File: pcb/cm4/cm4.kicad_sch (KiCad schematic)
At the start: 2 parts, among them J101 Conn_01x05, J102 Conn_01x07

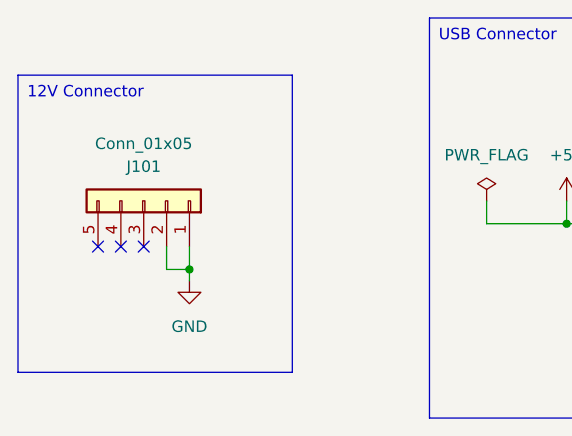
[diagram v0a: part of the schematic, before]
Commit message: fix power pin issue
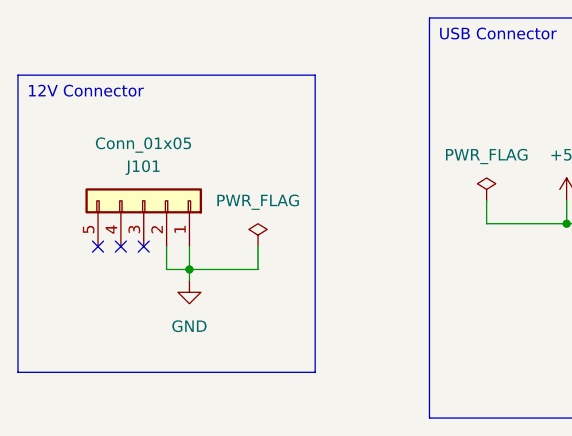
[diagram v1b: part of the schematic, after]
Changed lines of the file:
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@@
+	(wire
+		(pts
+			(xy 85.09 91.44) (xy 92.71 91.44)
+		)
+		(stroke
+			(width 0)
+			(type default)
+		)
+	)
 	(wire
 		(pts
@@
 	(wire
 		(pts
+			(xy 92.71 88.9) (xy 92.71 91.44)
+		)
+		(stroke
+			(width 0)
+			(type default)
+		)
+	)
+	(wire
+		(pts
 			(xy 85.09 91.44) (xy 85.09 92.71)
 		)
@@
 		(exclude_from_sim no)
 		(at 66.04 69.85 0)
-		(size 30.48 33.02)
+		(size 33.02 33.02)
 		(stroke
 			(width 0)
@@
 					(unit 1)
 				)
+			)
+		)
+	)
+	(symbol
+		(lib_id "power:PWR_FLAG")
+		(at 92.71 88.9 0)
+		(unit 1)
+		(exclude_from_sim no)
+		(in_bom yes)
+		(on_board yes)
+		(dnp no)
+		(fields_autoplaced yes)
+		(property "Reference" "#FLG0102"
+			(at 92.71 86.995 0)
+			(effects
+				(font
+					(size 1.27 1.27)
+				)
+				(hide yes)
+			)
+		)
+		(property "Value" "PWR_FLAG"
+			(at 92.71 83.82 0)
+			(effects
+				(font
+					(size 1.27 1.27)
+				)
+			)
+		)
+		(property "Footprint" ""
+			(at 92.71 88.9 0)
+			(effects
+				(font
+					(size 1.27 1.27)
+				)
+				(hide yes)
+			)
+		)
+		(property "Datasheet" "~"
+			(at 92.71 88.9 0)
+			(effects
+				(font
+					(size 1.27 1.27)
+				)
+				(hide yes)
+			)
+		)
+		(property "Description" "Special symbol for telling ERC where power comes from"
+			(at 92.71 88.9 0)
+			(effects
+				(font
+					(size 1.27 1.27)
+				)
+				(hide yes)
+			)
+		)
+		(pin "1"
+		)
+		(instances
+			(project "cm4"
+				(path "/5d20b266-567e-45c6-9e3e-145c2aea1daa"
+					(reference "#FLG0102")
+					(unit 1)
+				)

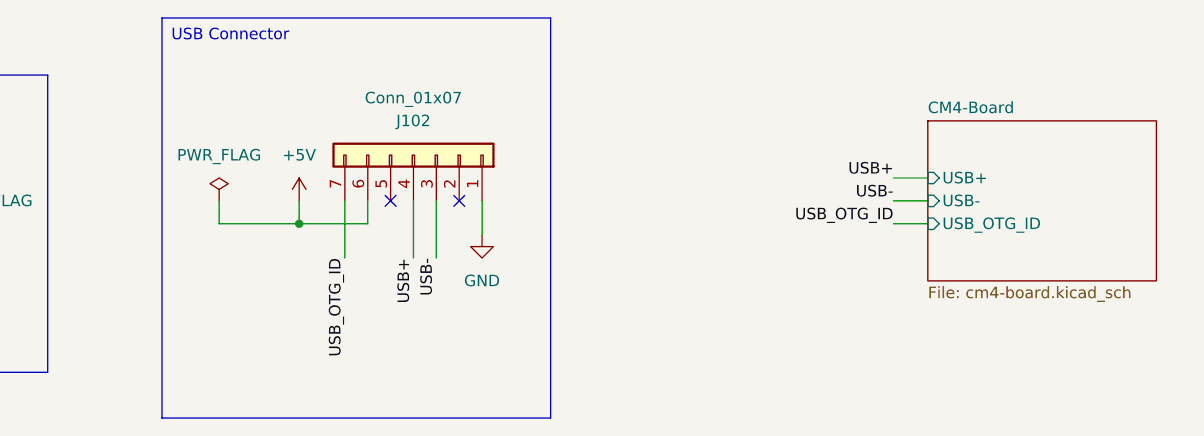
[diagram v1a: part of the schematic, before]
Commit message: update connectors
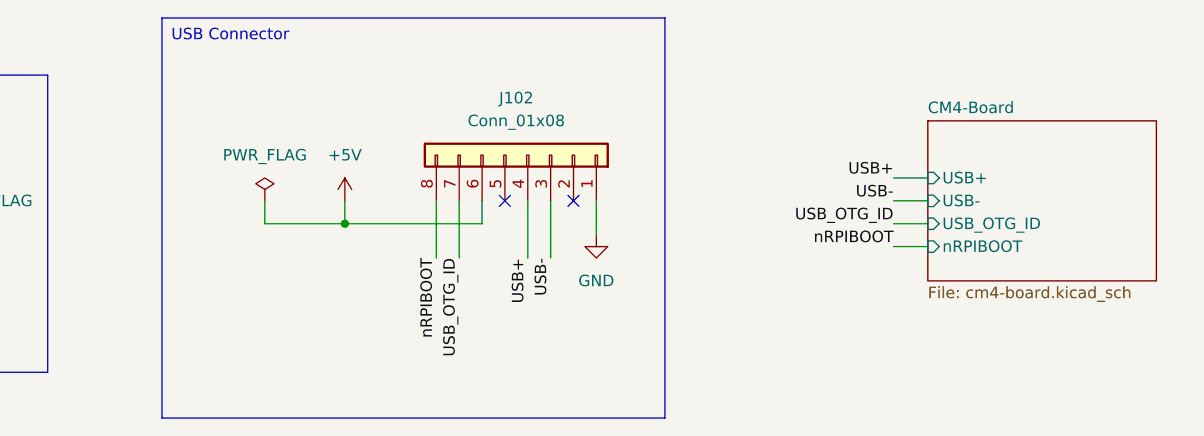
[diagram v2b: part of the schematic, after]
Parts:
- removed J102: Conn_01x07, symbol Connector_Generic:Conn_01x07
- added J102: Conn_01x08, symbol Connector_Generic:Conn_01x08
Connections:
- net +5V: now also J102.6 (Pin_6)
- net GND: now also J102.1 (Pin_1)
- net USB+: now also J102.4 (Pin_4)
- net USB-: now also J102.3 (Pin_3)
- net USB_OTG_ID: now also J102.7 (Pin_7)
- new net nRPIBOOT: J102.8 (Pin_8)
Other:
- sheet CM4-Board ports: added nRPIBOOT; removed none
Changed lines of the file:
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@@
 	)
 	(junction
-		(at 127 86.36)
+		(at 132.08 86.36)
 		(diameter 0)
 		(color 0 0 0 0)
@@
 	)
 	(no_connect
-		(at 137.16 83.82)
+		(at 149.86 83.82)
 	)
 	(no_connect
-		(at 144.78 83.82)
+		(at 157.48 83.82)
 	)
 	(no_connect
@@
 	(wire
 		(pts
-			(xy 139.7 90.17) (xy 139.7 83.82)
-		)
-		(stroke
-			(width 0)
-			(type default)
-		)
-	)
-	(wire
-		(pts
-			(xy 118.11 83.82) (xy 118.11 86.36)
-		)
-		(stroke
-			(width 0)
-			(type default)
-		)
-	)
-	(wire
-		(pts
-			(xy 127 83.82) (xy 127 86.36)
-		)
-		(stroke
-			(width 0)
-			(type default)
-		)
-	)
-	(wire
-		(pts
-			(xy 147.32 83.82) (xy 147.32 87.63)
+			(xy 152.4 90.17) (xy 152.4 83.82)
+		)
+		(stroke
+			(width 0)
+			(type default)
+		)
+	)
+	(wire
+		(pts
+			(xy 123.19 83.82) (xy 123.19 86.36)
+		)
+		(stroke
+			(width 0)
+			(type default)
+		)
+	)
+	(wire
+		(pts
+			(xy 132.08 83.82) (xy 132.08 86.36)
+		)
+		(stroke
+			(width 0)
+			(type default)
+		)
+	)
+	(wire
+		(pts
+			(xy 193.04 88.9) (xy 196.85 88.9)
+		)
+		(stroke
+			(width 0)
+			(type default)
+		)
+	)
+	(wire
+		(pts
+			(xy 160.02 83.82) (xy 160.02 87.63)
+		)
+		(stroke
+			(width 0)
+			(type default)
+		)
+	)
+	(wire
+		(pts
+			(xy 142.24 83.82) (xy 142.24 90.17)
 		)
 		(stroke
@@
 	(wire
 		(pts
-			(xy 134.62 83.82) (xy 134.62 86.36)
-		)
-		(stroke
-			(width 0)
-			(type default)
-		)
-	)
-	(wire
-		(pts
-			(xy 118.11 86.36) (xy 127 86.36)
-		)
-		(stroke
-			(width 0)
-			(type default)
-		)
-	)
-	(wire
-		(pts
-			(xy 142.24 90.17) (xy 142.24 83.82)
+			(xy 147.32 83.82) (xy 147.32 86.36)
+		)
+		(stroke
+			(width 0)
+			(type default)
+		)
+	)
+	(wire
+		(pts
+			(xy 123.19 86.36) (xy 132.08 86.36)
+		)
+		(stroke
+			(width 0)
+			(type default)
+		)
+	)
+	(wire
+		(pts
+			(xy 154.94 90.17) (xy 154.94 83.82)
 		)
 		(stroke
@@
 	(wire
 		(pts
-			(xy 134.62 86.36) (xy 127 86.36)
+			(xy 147.32 86.36) (xy 132.08 86.36)
 		)
 		(stroke
@@
 	(wire
 		(pts
-			(xy 132.08 83.82) (xy 132.08 90.17)
+			(xy 144.78 83.82) (xy 144.78 90.17)
 		)
 		(stroke
@@
 		(exclude_from_sim no)
 		(at 111.76 63.5 0)
-		(size 43.18 44.45)
+		(size 55.88 44.45)
 		(stroke
 			(width 0)
@@
 	)
 	(label "USB_OTG_ID"
-		(at 132.08 90.17 270)
+		(at 144.78 90.17 270)
 		(fields_autoplaced yes)
 		(effects
@@
 	)
 	(label "USB+"
-		(at 139.7 90.17 270)
+		(at 152.4 90.17 270)
 		(fields_autoplaced yes)
 		(effects
@@
 		)
 	)
+	(label "nRPIBOOT"
+		(at 193.04 88.9 180)
+		(fields_autoplaced yes)
+		(effects
+			(font
+				(size 1.27 1.27)
+			)
+			(justify right bottom)
+		)
+	)
+	(label "nRPIBOOT"
+		(at 142.24 90.17 270)
+		(fields_autoplaced yes)
+		(effects
+			(font
+				(size 1.27 1.27)
+			)
+			(justify right bottom)
+		)
+	)
 	(label "USB-"
-		(at 142.24 90.17 270)
+		(at 154.94 90.17 270)
 		(fields_autoplaced yes)
 		(effects
@@
 	(symbol
 		(lib_id "power:GND")
-		(at 147.32 87.63 0)
+		(at 160.02 87.63 0)
 		(unit 1)
 		(exclude_from_sim no)
@@
 		(fields_autoplaced yes)
 		(property "Reference" "#PWR0103"
-			(at 147.32 93.98 0)
+			(at 160.02 93.98 0)
 			(effects
 				(font
@@
 		)
 		(property "Value" "GND"
-			(at 147.32 92.71 0)
+			(at 160.02 92.71 0)
 			(effects
 				(font
@@
 		)
 		(property "Footprint" ""
-			(at 147.32 87.63 0)
+			(at 160.02 87.63 0)
 			(effects
 				(font
@@
 		)
 		(property "Datasheet" ""
-			(at 147.32 87.63 0)
+			(at 160.02 87.63 0)
 			(effects
 				(font
@@
 		)
 		(property "Description" "Power symbol creates a global label with name \"GND\" , ground"
-			(at 147.32 87.63 0)
+			(at 160.02 87.63 0)
 			(effects
 				(font
@@
 	)
 	(symbol
-		(lib_id "Connector_Generic:Conn_01x07")
-		(at 139.7 78.74 270)
+		(lib_id "Connector_Generic:Conn_01x08")
+		(at 152.4 78.74 270)
 		(mirror x)
 		(unit 1)
@@
 		(dnp no)
 		(property "Reference" "J102"
-			(at 139.7 74.93 90)
-			(effects
-				(font
-					(size 1.27 1.27)
-				)
-			)
-		)
-		(property "Value" "Conn_01x07"
-			(at 139.7 72.39 90)
+			(at 151.13 72.39 90)
+			(effects
+				(font
+					(size 1.27 1.27)
+				)
+			)
+		)
+		(property "Value" "Conn_01x08"
+			(at 151.13 74.93 90)
 			(effects
 				(font
@@
 		)
 		(property "Footprint" ""
-			(at 139.7 78.74 0)
+			(at 152.4 78.74 0)
 			(effects
 				(font
@@
 		)
 		(property "Datasheet" "~"
-			(at 139.7 78.74 0)
-			(effects
-				(font
-					(size 1.27 1.27)
-				)
-				(hide yes)
-			)
-		)
-		(property "Description" "Generic connector, single row, 01x07, script generated (kicad-library-utils/schlib/autogen/connector/)"
-			(at 139.7 78.74 0)
-			(effects
-				(font
-					(size 1.27 1.27)
-				)
-				(hide yes)
-			)
+			(at 152.4 78.74 0)
+			(effects
+				(font
+					(size 1.27 1.27)
+				)
+				(hide yes)
+			)
+		)
+		(property "Description" "Generic connector, single row, 01x08, script generated (kicad-library-utils/schlib/autogen/connector/)"
+			(at 152.4 78.74 0)
+			(effects
+				(font
+					(size 1.27 1.27)
+				)
+				(hide yes)
+			)
+		)
+		(pin "2"
 		)
 		(pin "3"
 		)
+		(pin "7"
+		)
+		(pin "6"
+		)
+		(pin "4"
+		)
+		(pin "1"
+		)
+		(pin "8"
+		)
 		(pin "5"
-		)
-		(pin "2"
-		)
-		(pin "4"
-		)
-		(pin "1"
-		)
-		(pin "6"
-		)
-		(pin "7"
 		)
 		(instances
@@
 	(symbol
 		(lib_id "power:+5V")
-		(at 127 83.82 0)
+		(at 132.08 83.82 0)
 		(unit 1)
 		(exclude_from_sim no)
@@
 		(fields_autoplaced yes)
 		(property "Reference" "#PWR0102"
-			(at 127 87.63 0)
+			(at 132.08 87.63 0)
 			(effects
 				(font
@@
 		)
 		(property "Value" "+5V"
-			(at 127 78.74 0)
+			(at 132.08 78.74 0)
 			(effects
 				(font
@@
 		)
 		(property "Footprint" ""
-			(at 127 83.82 0)
+			(at 132.08 83.82 0)
 			(effects
 				(font
@@
 		)
 		(property "Datasheet" ""
-			(at 127 83.82 0)
+			(at 132.08 83.82 0)
 			(effects
 				(font
@@
 		)
 		(property "Description" "Power symbol creates a global label with name \"+5V\""
-			(at 127 83.82 0)
+			(at 132.08 83.82 0)
 			(effects
 				(font
@@
 	(symbol
 		(lib_id "power:PWR_FLAG")
-		(at 118.11 83.82 0)
+		(at 123.19 83.82 0)
 		(unit 1)
 		(exclude_from_sim no)
@@
 		(fields_autoplaced yes)
 		(property "Reference" "#FLG0101"
-			(at 118.11 81.915 0)
+			(at 123.19 81.915 0)
 			(effects
 				(font
@@
 		)
 		(property "Value" "PWR_FLAG"
-			(at 118.11 78.74 0)
+			(at 123.19 78.74 0)
 			(effects
 				(font
@@
 		)
 		(property "Footprint" ""
-			(at 118.11 83.82 0)
+			(at 123.19 83.82 0)
 			(effects
 				(font
@@
 		)
 		(property "Datasheet" "~"
-			(at 118.11 83.82 0)
+			(at 123.19 83.82 0)
 			(effects
 				(font
@@
 		)
 		(property "Description" "Special symbol for telling ERC where power comes from"
-			(at 118.11 83.82 0)
+			(at 123.19 83.82 0)
 			(effects
 				(font
@@
 			(effects
 				(font
+					(size 1.27 1.27)
+				)
+				(justify left)
+			)
+		)
+		(pin "nRPIBOOT" input
+			(at 196.85 88.9 180)
+			(effects
+				(font

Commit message: update cm4
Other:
- added sheet Ethernet (ethernet.kicad_sch)
- added sheet MicroSD (micro_sd.kicad_sch)
- sheet CM4-Board ports: added ETH_GREEN, ETH_YELLOW, SD_CLK, SD_CMD, SD_DATA0, SD_DATA1, SD_DATA2, SD_DATA3, SD_PWR_ON, TRD0+, TRD0-, TRD1+, TRD1-, TRD2+, TRD2-, TRD3+, TRD3-; removed none
- moved on the sheet: J101, J102

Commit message: update pcb
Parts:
- J101: footprint (none) -> Connector_PinHeader_2.54mm:PinHeader_1x05_P2.54mm_Horizontal
- J102: footprint (none) -> Connector_PinHeader_2.54mm:PinHeader_1x08_P2.54mm_Horizontal
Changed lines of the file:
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@@
 			)
 		)
-		(property "Footprint" ""
+		(property "Footprint" "Connector_PinHeader_2.54mm:PinHeader_1x05_P2.54mm_Horizontal"
 			(at 49.53 101.6 0)
 			(effects
@@
 		)
 		(property "Description" "Generic connector, single row, 01x05, script generated (kicad-library-utils/schlib/autogen/connector/)"
+			(at 49.53 101.6 0)
+			(effects
+				(font
+					(size 1.27 1.27)
+				)
+				(hide yes)
+			)
+		)
+		(property "LCSC" ""
 			(at 49.53 101.6 0)
 			(effects
@@
 			)
 		)
-		(property "Footprint" ""
+		(property "Footprint" "Connector_PinHeader_2.54mm:PinHeader_1x08_P2.54mm_Horizontal"
 			(at 121.92 96.52 0)
 			(effects
@@
 			)
 		)
+		(property "LCSC" ""
+			(at 121.92 96.52 0)
+			(effects
+				(font
+					(size 1.27 1.27)
+				)
+				(hide yes)
+			)
+		)
 		(pin "2"
 		)
@@
 		(dnp no)
 		(fields_autoplaced yes)
-		(property "Reference" "#FLG0102"
+		(property "Reference" "#FLG0101"
 			(at 62.23 104.775 0)
 			(effects
@@
 			(project "cm4"
 				(path "/5d20b266-567e-45c6-9e3e-145c2aea1daa"
-					(reference "#FLG0102")
+					(reference "#FLG0101")
 					(unit 1)
 				)
@@
 		(dnp no)
 		(fields_autoplaced yes)
-		(property "Reference" "#FLG0101"
+		(property "Reference" "#FLG0102"
 			(at 92.71 99.695 0)
 			(effects
@@
 			(project "cm4"
 				(path "/5d20b266-567e-45c6-9e3e-145c2aea1daa"
-					(reference "#FLG0101")
-					(unit 1)
-				)
+					(reference "#FLG0102")
+					(unit 1)
+				)

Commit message: update cm4 board
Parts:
- J101: LCSC (none) -> C492413
- J102: LCSC (none) -> C706871
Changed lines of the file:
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@@
 			)
 		)
-		(property "LCSC" ""
+		(property "LCSC" "C492413"
 			(at 49.53 101.6 0)
 			(effects
@@
 			)
 		)
-		(property "LCSC" ""
+		(property "LCSC" "C706871"
 			(at 121.92 96.52 0)
 			(effects

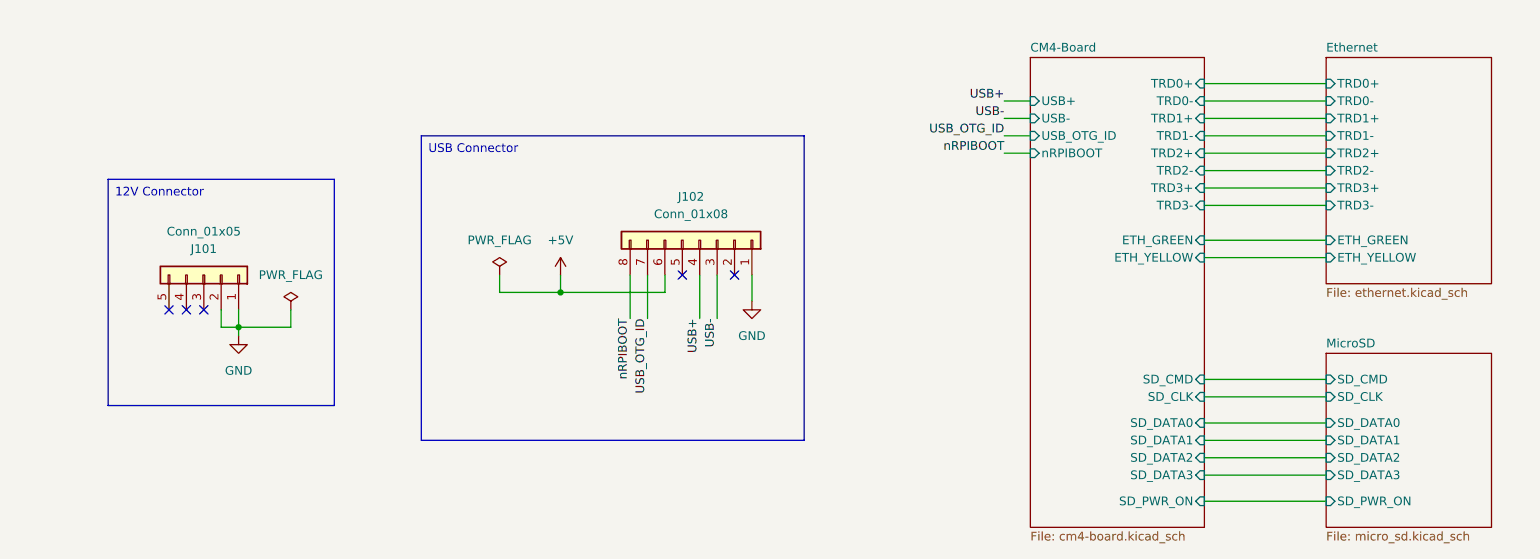
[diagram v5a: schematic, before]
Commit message: cm4: update footprint library, add 3d files, update dimensions
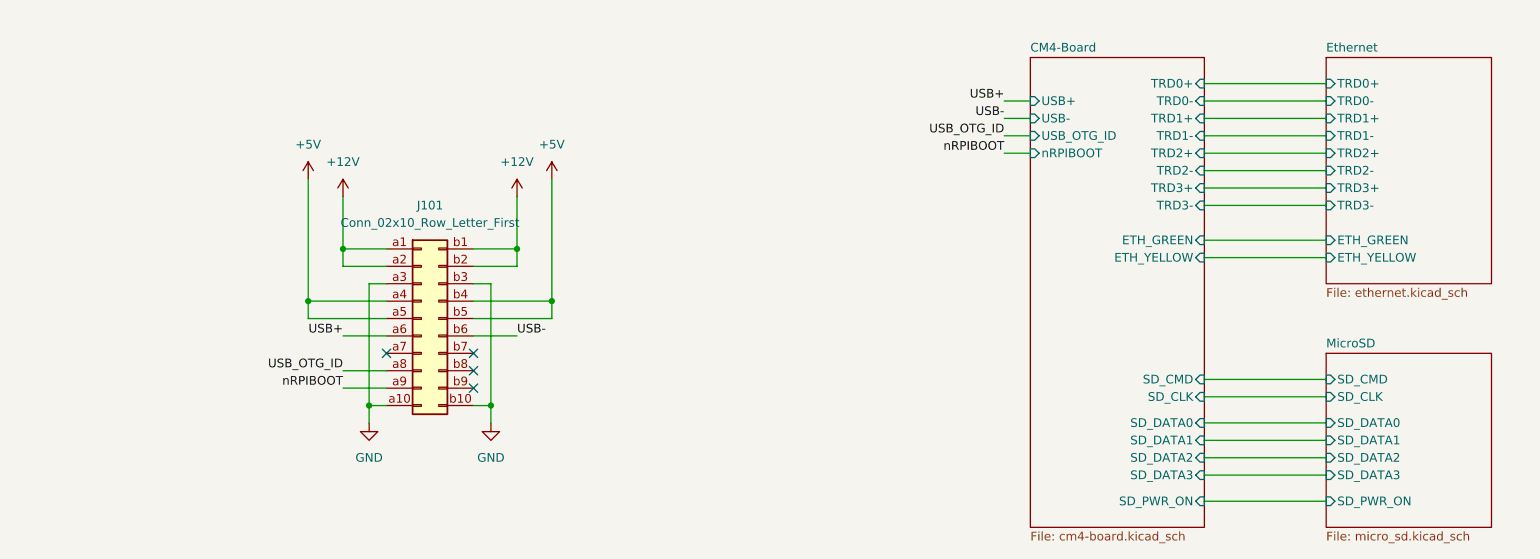
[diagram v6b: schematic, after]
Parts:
- removed J101: Conn_01x05, Connector_PinHeader_2.54mm:PinHeader_1x05_P2.54mm_Horizontal, symbol Connector_Generic:Conn_01x05
- removed J102: Conn_01x08, Connector_PinHeader_2.54mm:PinHeader_1x08_P2.54mm_Horizontal, symbol Connector_Generic:Conn_01x08
- added J101: Conn_02x10_Row_Letter_First, PRJ:PCN10C-20S-2.54DS, symbol Connector_Generic:Conn_02x10_Row_Letter_First
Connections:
- net +5V: now also J101.a4 (Pin_a4), J101.a5 (Pin_a5), J101.b4 (Pin_b4), J101.b5 (Pin_b5)
- net GND: now also J101.a10 (Pin_a10), J101.a3 (Pin_a3), J101.b10 (Pin_b10), J101.b3 (Pin_b3)
- net USB+: now also J101.a6 (Pin_a6)
- net USB-: now also J101.b6 (Pin_b6)
- net USB_OTG_ID: now also J101.a8 (Pin_a8)
- net nRPIBOOT: now also J101.a9 (Pin_a9)
- new net +12V: J101.a1 (Pin_a1), J101.a2 (Pin_a2), J101.b1 (Pin_b1), J101.b2 (Pin_b2)
- no-connect marks 5 -> 4

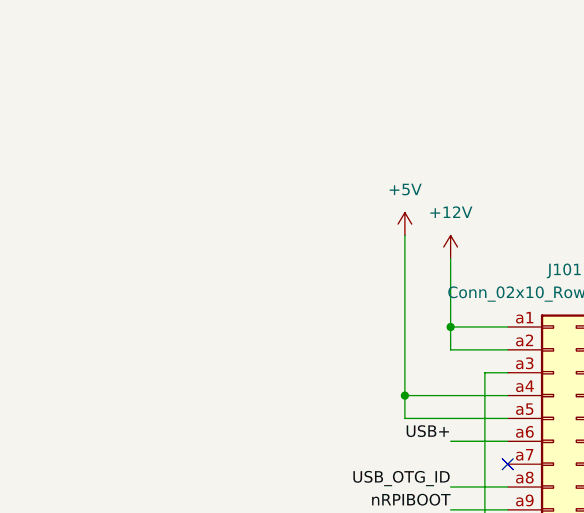
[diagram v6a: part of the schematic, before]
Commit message: fix power pins
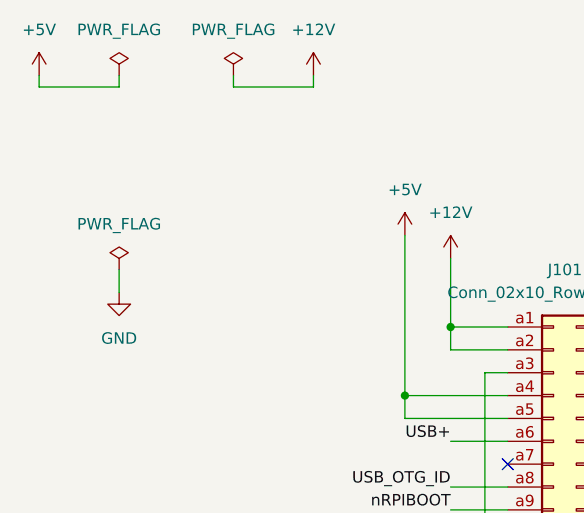
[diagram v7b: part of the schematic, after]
